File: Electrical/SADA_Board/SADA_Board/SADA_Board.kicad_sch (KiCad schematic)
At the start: 28 parts, among them J1 644752-2, U1 XC6230A001QR-G, U2 Si1442DH, U5 pico_shield

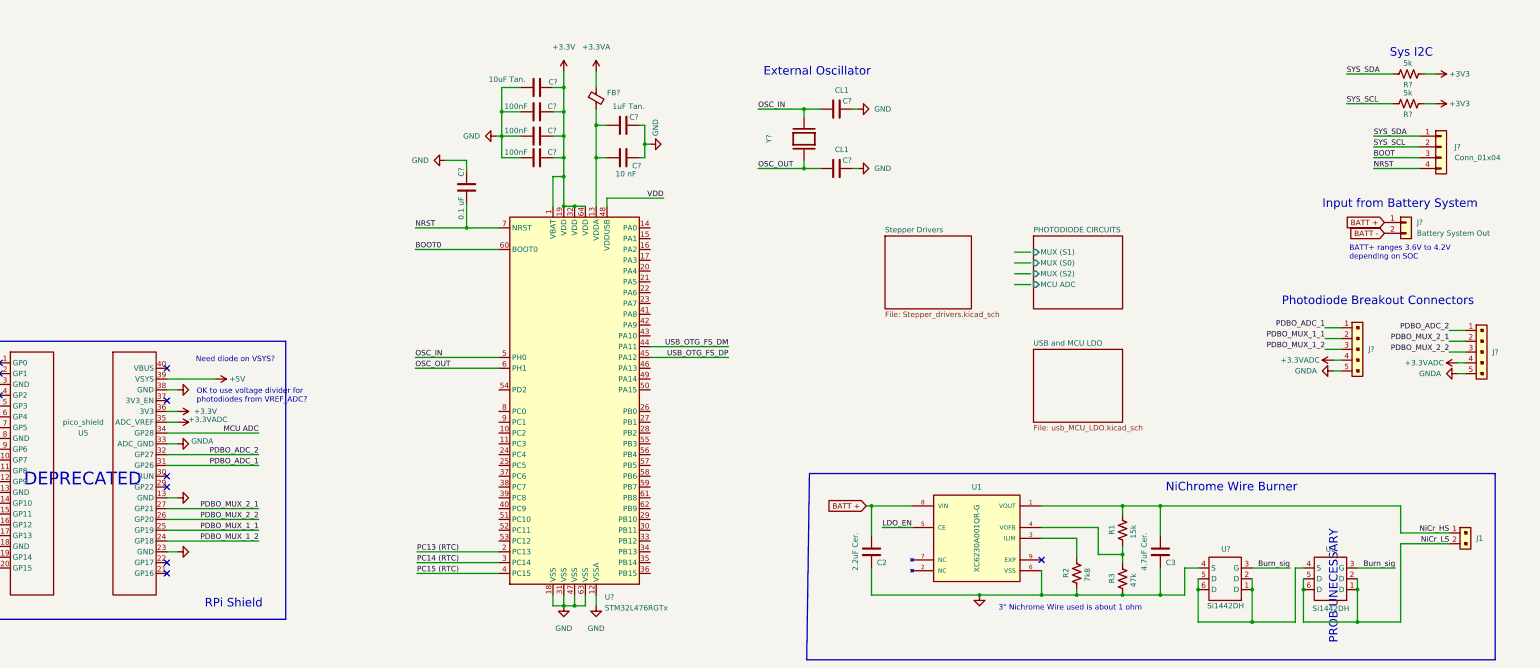
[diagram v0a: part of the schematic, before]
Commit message: Partial implementation of stepper motor Step up
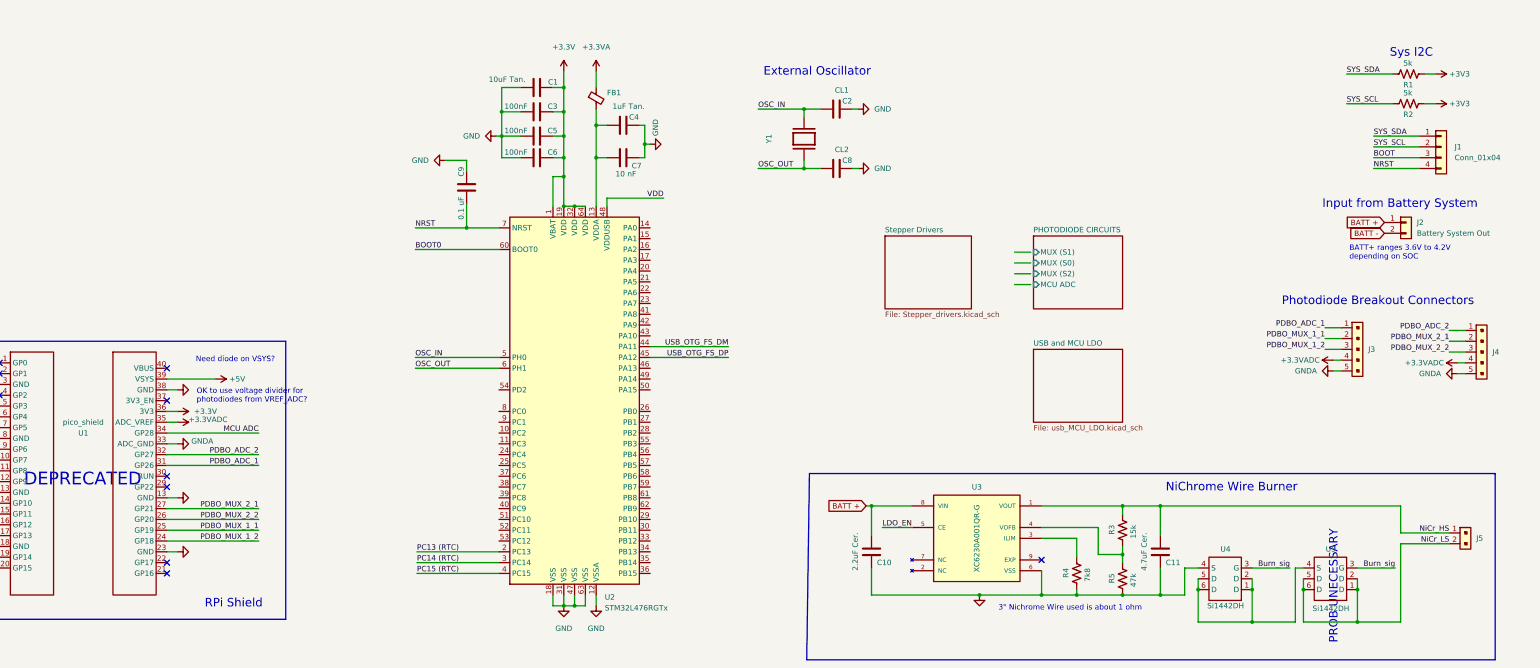
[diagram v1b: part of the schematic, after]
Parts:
- C8: renamed from C?; value CL1 -> CL2
- gave numbers to parts that had none: 18
- renumbered C2 to C10, C3 to C11, J1 to J5, R1 to R3, R2 to R4, R3 to R5, U5 to U1, U1 to U3, U2 to U5

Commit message: Rough draft stepup done
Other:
- note added: "TODO: - mosfet for stepper power (HS to keep ground connected) - Headers for all GPIO pins - Jumpers? - Hierarchal labels- may need to put 3V3 and others as global? - Connect grounds of System and SADA Board? Twisted pairs with ground? - current sensing? - Grounding Considerations... Do I just directly connect BATT- to ground or is there some sort of star grounding that should occur? future: - gi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"
- note removed: "TODO: - mosfet for stepper power (HS to keep ground connected) - Power considerations- input from battery/systems board, then filtering, then stepup. Standard - do things need to be at 5V other than stepper? maybe we could just use 3.3V - Stepper driver... is this final? what is the actual motor we are using? - Headers for all GPIO pins - Jumpers? - Hierarchal labels- may need to put 3V3 and othe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"

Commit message: Connectors, Oscillator
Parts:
- removed C3, C5: 100nF, Capacitor_SMD:C_0603_1608Metric, symbol Device:C
- removed C8: CL2, Capacitor_SMD:C_0603_1608Metric, symbol Device:C
- removed C9: 0.1 uF, Capacitor_SMD:C_0603_1608Metric, symbol Device:C
- removed FB1: FerriteBead_Small, symbol Device:FerriteBead_Small
- removed J1: Conn_01x04, symbol Connector_Generic:Conn_01x04
- removed J2: Battery System Out, symbol Connector_Generic:Conn_01x02
- removed J3, J4: B5B-XH-A_LF__SN_, digikey-footprints:PinHeader_1x5_P2.5mm_Drill1.1mm, symbol dk_Rectangular-Connectors-Headers-Male-Pins:B5B-XH-A_LF__SN_
- removed J5: 644752-2, digikey-footprints:PinHeader_1x2_P2mm_Drill1mm, symbol dk_Rectangular-Connectors-Headers-Male-Pins:B2B-PH-K-S_LF__SN_
- removed R2: 5k, symbol Device:R_US
- removed U1: pico_shield, symbol pi_pico_shield:pico_shield
- removed U5: Si1442DH, Package_TO_SOT_SMD:SOT-363_SC-70-6, symbol 0_custom:Si1442DH
- removed Y1: XRCGB48M000F5A00R0, OSC_XRCGB48M000F5A00R0, symbol XRCGB48M000F5A00R0:XRCGB48M000F5A00R0
- added C12: C, symbol Device:C
- added C? (x3): 100nF, Capacitor_SMD:C_0603_1608Metric, symbol Device:C
- added C?: CL2, Capacitor_SMD:C_0402_1005Metric, symbol Device:C
- added EXT? (x3): Male Conn., 0_custom:EXT_no_footprint, symbol 0_custom:{lt}name{gt}
- added J2, J? (x2): Conn_01x04, Miles Added:1719730004, symbol Connector_Generic:Conn_01x04
- added J?: 105431-1202, Miles Added:1054311202, symbol molex_105431-1202:105431-1202
- added R1: 4.7k, Resistor_SMD:R_0402_1005Metric, symbol Device:R_US
- added R6: r, symbol Device:R_US
- added Y?: ECS_Chrystal_, 0_custom:ECS-XTAL-5.0x3.2, symbol 0_custom:ECS_Chrystal_
- C1: MPN (none) -> F981A106MMUAJ6
- C10: footprint Capacitor_SMD:C_0805_2012Metric -> Capacitor_SMD:C_0603_1608Metric; MPN CL21B225KOFVPNE -> CGA3E1X7S1C225M080AC
- C11: footprint Capacitor_SMD:C_0805_2012Metric -> Capacitor_SMD:C_0603_1608Metric; MPN C2012X7R1A475K125AC -> GRT188C71C475KE13D
- C2: footprint Capacitor_SMD:C_0603_1608Metric -> Capacitor_SMD:C_0402_1005Metric; MPN (none) -> CGA2B2C0G1H060D050BA
- C4: MPN (none) -> TACL105K016XTA
- C6: MPN (none) -> C0603X104K3RAC7867
- R2: renamed from R1; value 5k -> 4.7k; footprint (none) -> Resistor_SMD:R_0402_1005Metric; MPN (none) -> AC0402FR-134K7L
- R3: footprint Resistor_SMD:R_0805_2012Metric_Pad1.20x1.40mm_HandSolder -> Resistor_SMD:R_0603_1608Metric; MPN RMCF0805FT15K8 -> AC0603FR-0715KL
- R4: value 7k8 -> 7.5k; footprint Resistor_SMD:R_0805_2012Metric_Pad1.20x1.40mm_HandSolder -> Resistor_SMD:R_0603_1608Metric_Pad0.98x0.95mm_HandSolder; MPN RC0805FR-077K87L -> AC0603FR-077K5L
- R5: footprint Resistor_SMD:R_0805_2012Metric_Pad1.20x1.40mm_HandSolder -> Resistor_SMD:R_0603_1608Metric; MPN RC0805FR-1347KL -> AC0603FR-1047KL
- renumbered U2 to U1, U3 to U2, U4 to U3
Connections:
- net VDD is gone; now on net +3.3V: U1.48 (VDDUSB)
- net +3.3V: now also C4.2, C7.2, U1.13 (VDDA), C?.1, C?.1
- net +3V3: now also J2.3 (Pin_3), J?.3 (Pin_3), R1.1
- net BOOT: now also J?.3 (Pin_3)
- net GND: now also C?.1, C?.1, C?.2, C?.2, J2.4 (Pin_4), J?.4 (Pin_4), J?.MP1, J?.MP2, Y?.2 (GND), Y?.4 (GND)
- net NRST: now also C?.2, J?.4 (Pin_4)
- net NiCr_HS: now also J?.1
- net NiCr_LS: now also U3.1 (D), U3.2 (D), U3.5 (D), U3.6 (D), J?.2
- net OSC_IN: now also Y?.3 (OUT/IN)
- net OSC_OUT: now also C?.2, Y?.1 (IN/OUT)
- net SYS_SCL: now also U1.58 (PB6), J?.1 (Pin_1), R1.2
- net SYS_SDA: now also U1.59 (PB7), J?.2 (Pin_2)
- net STEP_VREF2: now reaches U1.22 (PA6)
- net MTR2_DIR: now reaches U1.23 (PA7)
- net STEP_VREF1: now reaches U1.37 (PC6)
- net MTR1_STCK: now reaches U1.38 (PC7)
- net MTR1_DIR: now reaches U1.39 (PC8)
- net MTR1_FAULT: now reaches U1.40 (PC9)
- net MTR2_STCK: now reaches U1.41 (PA8)
- net MTR2_FAULT: now reaches U1.42 (PA9)
- net MTR2_STBY: now reaches U1.43 (PA10)
- net MTR1_STBY: now reaches U1.51 (PC10)
- new net PhDio_AUX_SCL: J2.1 (Pin_1), J?.1 (Pin_1)
- new net PhDio_AUX_SDA: J2.2 (Pin_2), J?.2 (Pin_2)
- no-connect marks 10 -> 1
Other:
- sheet PHOTODIODE CIRCUITS renamed CRNR PHOTODIODES
- removed sheet Stepper Drivers
- added sheet Steppers (Bipolar_Steppers.kicad_sch)
- sheet USB and MCU LDO ports: added USB_OTG_FS_DM, USB_OTG_FS_DP; removed none
- note added: "Passive Retainment NiChrome Burner"
- note added: "SCHEMATIC NOTES - See subpages for specific notes - BATT+ ranges 3.6V to 4.2V depending on SOC - Passive Retainment: 3" Nichrome Wire used is about 1 ohm"
- note added: "STM32 L476 MCU"
- note added: "TODO: - Headers for some GPIO pins - Jumpers? - Need to exchange ground with system board? - current sensing? - Star grounding? Ground loops anywhere? - grounding to chassis - SMD Shields"
- note added: "TODO: - update all connectors - find clock - power budget sheet - 3v3 LDO - USB Impedence - change aux photodiode board to i2c - double check flyback diodes on steppers"
- note removed: "3" Nichrome Wire used is about 1 ohm"
- note removed: "BATT+ ranges 3.6V to 4.2V depending on SOC"
- note removed: "DEPRECATED"
- note removed: "Input from Battery System"
- note removed: "Need diode on VSYS?"
- note removed: "NiChrome Wire Burner"
- note removed: "OK to use voltage divider for photodiodes from VREF_ADC?"
- note removed: "PROB UNECESSARY"
- note removed: "RPi Shield"
- note removed: "TODO: - mosfet for stepper power (HS to keep ground connected) - Headers for all GPIO pins - Jumpers? - Hierarchal labels- may need to put 3V3 and others as global? - Connect grounds of System and SADA Board? Twisted pairs with ground? - current sensing? - Grounding Considerations... Do I just directly connect BATT- to ground or is there some sort of star grounding that should occur? future: - gi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"
- moved on the sheet: C10, C11, C2, R2, R3, R4, R5, U2, U3

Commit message: Pre-Design Review II
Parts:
- removed C10: 2.2uF Cer., Capacitor_SMD:C_0603_1608Metric, symbol Device:C
- removed C11: 4.7uF Cer., Capacitor_SMD:C_0603_1608Metric, symbol Device:C
- removed C12: C, symbol Device:C
- removed J?: 105431-1202, Miles Added:1054311202, symbol molex_105431-1202:105431-1202
- removed R3: 15k, Resistor_SMD:R_0603_1608Metric, symbol Device:R_US
- removed R4: 7.5k, Resistor_SMD:R_0603_1608Metric_Pad0.98x0.95mm_HandSolder, symbol Device:R_US
- removed R5: 47k, Resistor_SMD:R_0603_1608Metric, symbol Device:R_US
- removed R6: r, symbol Device:R_US
- removed U2: XC6230A001QR-G, SOIC127P600X175-9N, symbol XC6230A001QR-G:XC6230A001QR-G
- removed U3: Si1442DH, Package_TO_SOT_SMD:SOT-363_SC-70-6, symbol 0_custom:Si1442DH
- added J?: Headers, Connector_PinSocket_2.00mm:PinSocket_2x30_P2.00mm_Vertical, symbol Connector_Generic:Conn_02x30_Counter_Clockwise
- added J?: Conn_01x05, Connector_PinSocket_2.00mm:PinSocket_1x05_P2.00mm_Vertical, symbol Connector_Generic:Conn_01x05
- J2: value Conn_01x04 -> Aux. Photodiode Board 1
- J?: value Conn_01x04 -> Systems Board Connector
- J?: value Conn_01x04 -> Aux. Photodiode Board 2
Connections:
- net PhDio_AUX_SCL is gone; now on net SYS_SCL: J2.1 (Pin_1), J?.1 (Pin_1)
- net PhDio_AUX_SDA is gone; now on net SYS_SDA: J2.2 (Pin_2), J?.2 (Pin_2)
- net +3V3: now also J?.47 (Pin_47), J?.48 (Pin_48)
- net BATT +: now also J?.12 (Pin_12), J?.13 (Pin_13)
- net BOOT0: now also J?.60 (Pin_60)
- net Burn_sig: now also U1.11 (PC3), J?.11 (Pin_11)
- net GND: now also J?.18 (Pin_18), J?.19 (Pin_19), J?.31 (Pin_31), J?.54 (Pin_54)
- net LDO_EN: now also U1.10 (PC2), J?.10 (Pin_10)
- net MTR1_DIR: now also J?.39 (Pin_39)
- net MTR1_FAULT: now also J?.40 (Pin_40)
- net MTR1_STBY: now also U1.36 (PB15), J?.36 (Pin_36); no longer U1.51 (PC10)
- net MTR1_STCK: now also J?.38 (Pin_38)
- net MTR2_DIR: now also U1.59 (PB7), J?.59 (Pin_59); no longer U1.23 (PA7)
- net MTR2_FAULT: now also U1.62 (PB9), J?.55 (Pin_55); no longer U1.42 (PA9)
- net MTR2_STBY: now also U1.57 (PB5), J?.57 (Pin_57); no longer U1.43 (PA10)
- net MTR2_STCK: now also U1.61 (PB8), J?.56 (Pin_56); no longer U1.41 (PA8)
- net MUX (S0): now also U1.27 (PB1), J?.27 (Pin_27)
- net MUX (S1): now also U1.28 (PB2), J?.28 (Pin_28)
- net MUX (S2): now also U1.25 (PC5), J?.25 (Pin_25)
- net NRST: now also J?.7 (Pin_7)
- net OSC_IN: now also J?.5 (Pin_5)
- net OSC_OUT: now also J?.6 (Pin_6)
- net PC13 (RTC): now also J?.2 (Pin_2)
- net PC14 (RTC): now also J?.3 (Pin_3)
- net PC15 (RTC): now also J?.4 (Pin_4)
- net STEP_VREF1: now also J?.37 (Pin_37)
- net STEP_VREF2: now also U1.58 (PB6), J?.58 (Pin_58); no longer U1.22 (PA6)
- net SYS_SCL: now also U1.8 (PC0), J?.8 (Pin_8); no longer U1.58 (PB6)
- net SYS_SDA: now also U1.9 (PC1), J?.9 (Pin_9); no longer U1.59 (PB7)
- net USB_OTG_FS_DM: now also J?.44 (Pin_44)
- net USB_OTG_FS_DP: now also J?.45 (Pin_45)
- net PA0: now reaches U1.14 (PA0)
- net PA0: now also J?.14 (Pin_14)
- net PA1: now reaches U1.15 (PA1)
- net PA1: now also J?.15 (Pin_15)
- net PA2: now reaches U1.16 (PA2)
- net PA2: now also J?.16 (Pin_16)
- net PA3: now reaches U1.17 (PA3)
- net PA3: now also J?.17 (Pin_17)
- net PA4: now reaches U1.20 (PA4)
- net PA4: now also J?.20 (Pin_20)
- net PA5: now reaches U1.21 (PA5)
- net PA5: now also J?.21 (Pin_21)
- net PC4: now reaches U1.24 (PC4)
- net PC4: now also J?.24 (Pin_24)
- net PhDio ADC: now reaches U1.26 (PB0)
- net PhDio ADC: now also J?.26 (Pin_26)
- net PB10: now reaches U1.29 (PB10)
- net PB10: now also J?.29 (Pin_29)
- net PB11: now reaches U1.30 (PB11)
- net PB11: now also J?.30 (Pin_30)
- net PB12: now reaches U1.33 (PB12)
- net PB12: now also J?.33 (Pin_33)
- net PB13: now reaches U1.34 (PB13)
- net PB13: now also J?.34 (Pin_34)
- net PB14: now reaches U1.35 (PB14)
- net PB14: now also J?.35 (Pin_35)
- net JTMS-SWDIO: now reaches U1.46 (PA13)
- net JTMS-SWDIO: now also J?.1 (Pin_1), J?.46 (Pin_46)
- net JTCK-SWCLK: now reaches U1.49 (PA14)
- net JTCK-SWCLK: now also J?.2 (Pin_2), J?.49 (Pin_49)
- net JTDI: now reaches U1.50 (PA15)
- net JTDI: now also J?.3 (Pin_3), J?.50 (Pin_50)
- net PC11: now reaches U1.52 (PC11)
- net PC11: now also J?.52 (Pin_52)
- net PC12: now reaches U1.53 (PC12)
- net PC12: now also J?.53 (Pin_53)
- net PD2: now reaches U1.54 (PD2)
- net JTDO - SWO: now reaches U1.55 (PB3)
- net JTDO - SWO: now also J?.4 (Pin_4)
- net NJTRST: now reaches U1.56 (PB4)
- net NJTRST: now also J?.5 (Pin_5)
- new net PA10: J?.43 (Pin_43), U1.43 (PA10)
- new net PA6: J?.22 (Pin_22), U1.22 (PA6)
- new net PA7: J?.23 (Pin_23), U1.23 (PA7)
- new net PA8: J?.41 (Pin_41), U1.41 (PA8)
- new net PA9: J?.42 (Pin_42), U1.42 (PA9)
- new net PC10: J?.51 (Pin_51), U1.51 (PC10)
- new net VDD: J?.1 (Pin_1), J?.32 (Pin_32)
- no-connect marks 1 -> 0
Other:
- sheet Steppers renamed Steppers 
- added sheet Passive Retainment (Passive_retainment.kicad_sch)
- note added: "Attitude Determination Photodiodes"
- note added: "Headers"
- note added: "JTAG/SWD"
- note added: "Passive Retainment"
- note added: "SCHEMATIC NOTES - See subpages for specific notes - BATT+ ranges 3.6V to 4.2V depending on SOC - Passive Retainment: 3" Nichrome Wire used is about 1 ohm - 'Headers' section will not be included on a final board, just for troubleshooting"
- note added: "Stepper Motors"
- note added: "System Board Interface"
- note added: "USB and 3V3 Power"
- note removed: "Passive Retainment NiChrome Burner"
- note removed: "SCHEMATIC NOTES - See subpages for specific notes - BATT+ ranges 3.6V to 4.2V depending on SOC - Passive Retainment: 3" Nichrome Wire used is about 1 ohm"
- note removed: "Sys I2C"
- note removed: "TODO: - Headers for some GPIO pins - Jumpers? - Need to exchange ground with system board? - current sensing? - Star grounding? Ground loops anywhere? - grounding to chassis - SMD Shields"
- note removed: "TODO: - update all connectors - find clock - power budget sheet - 3v3 LDO - USB Impedence - change aux photodiode board to i2c - double check flyback diodes on steppers"
- moved on the sheet: C2, C?, EXT?, J2, J?, R1, R2, Y?

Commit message: Pre-passive retainment change
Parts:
- removed C6, C? (x2): 100nF, Capacitor_SMD:C_0603_1608Metric, symbol Device:C
- added C? (x3): 100nF, Capacitor_SMD:C_0402_1005Metric, symbol Device:C
- C7: footprint Capacitor_SMD:C_0603_1608Metric -> Capacitor_SMD:C_0402_1005Metric; MPN (none) -> GRT155R71C103KE01J
- C?: footprint Capacitor_SMD:C_0603_1608Metric -> Capacitor_SMD:C_0402_1005Metric; MPN C0603X104K3RAC7867 -> GRT155R71C104KE01J
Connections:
- net +3.3V: now also C?.2, C?.2, C?.2
- net BOOT0: now also J?.31 (Pin_31); no longer J?.60 (Pin_60)
- net GND: now also J?.60 (Pin_60), C?.1, C?.1, C?.1; no longer J?.31 (Pin_31)
- net JTCK-SWCLK: no longer J?.49 (Pin_49)
- net JTDI: no longer J?.50 (Pin_50)
- net JTMS-SWDIO: no longer J?.46 (Pin_46)
- net SYS_SCL: now also J?.50 (Pin_50)
- net SYS_SDA: now also J?.49 (Pin_49)
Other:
- note added: "TODO: - USB research - GIO noise video - netlist check - passive retainment duplicate"

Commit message: pre-gio review
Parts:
- removed Y?: ECS_Chrystal_, 0_custom:ECS-XTAL-5.0x3.2, symbol 0_custom:ECS_Chrystal_
- added D1: TVS, symbol Diode:ESD5Zxx
- added D2, D3, D4, D5, D6, D7: TVS, Diode_SMD:D_0402_1005Metric, symbol Diode:ESD5Zxx
- added TP1, TP2, TP3, TP4: TestPoint, TestPoint:TestPoint_Pad_D1.5mm, symbol Connector:TestPoint
- added Y1: ECS_Chrystal_, Miles Added:XTAL_ECS-160-8-36Q-AES-TR, symbol 0_custom:ECS_Chrystal_
- gave numbers to parts that had none: 12
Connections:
- net +3.3V is gone; now on net +3V3: C1.1, C3.2, C4.2, C5.2, C6.2, C7.2, U1.1 (VBAT), U1.13 (VDDA), U1.19 (VDD), U1.32 (VDD), U1.48 (VDDUSB), U1.64 (VDD)
- net BOOT0 is gone; now on net BOOT: J1.31 (Pin_31), U1.60 (BOOT0)
- net +3V3: now also D1.1 (K)
- net BOOT: now also D3.1 (K)
- net GND: now also J1.46 (Pin_46), D1.2 (A), D2.2 (A), D3.2 (A), D4.2 (A), D5.2 (A), D6.2 (A), D7.2 (A), Y1.2 (GND), Y1.4 (GND); no longer J1.54 (Pin_54)
- net NRST: now also D2.1 (K)
- net OSC_IN: now also TP1.1, Y1.1 (IN/OUT)
- net OSC_OUT: now also TP2.1, Y1.3 (OUT/IN)
- net PD2: now also J1.54 (Pin_54)
- net SYS_SCL: now also D6.1 (K), TP3.1
- net SYS_SDA: now also D7.1 (K), TP4.1
- net USB_OTG_FS_DM: now also D4.1 (K)
- net USB_OTG_FS_DP: now also D5.1 (K)
- net LDO_EN renamed PR_EN
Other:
- sheet Passive Retainment ports: added PR_EN; removed LDO_EN
- note added: "TVS Diodes on clock?"
- note added: "TVS diodes? pins only used on ground charge could still build up though right?"
- note removed: "TODO: - USB research - GIO noise video - netlist check - passive retainment duplicate"
- title: CubeSat Pi Hat -> CubeSat SADA - Main
- moved on the sheet: C1, C3, C4, C5, C6, C7, C8, EXT3, J1, J5, R1, R2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

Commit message: ESD changes
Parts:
- added D28: LG_R971-KN-1, digikey-footprints:0805, symbol dk_LED-Indication-Discrete:LG_R971-KN-1
- added H1, H2, H3, H4: MountingHole_Pad, MountingHole:MountingHole_2.5mm_Pad, symbol Mechanical:MountingHole_Pad
- added JP1: Jumper_3_Open, Connector_PinHeader_2.54mm:PinHeader_1x03_P2.54mm_Vertical_SMD_Pin1Right, symbol Jumper:Jumper_3_Open
- added R31: 4.7k, Resistor_SMD:R_0402_1005Metric, symbol Device:R_US
- D1: footprint (none) -> Diode_SMD:D_0402_1005Metric; MPN (none) -> ESD321DPYR
- TP1, TP2, TP3, TP4: footprint TestPoint:TestPoint_Pad_D1.5mm -> TestPoint:TestPoint_Pad_D1.0mm
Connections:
- net +3V3: now also D28.1, JP1.3 (B)
- net BOOT: now also R31.1
- net GND: now also D28.2, H1.1, H2.1, H3.1, H4.1, JP1.1 (A)
- new net: JP1.2 (C), R31.2
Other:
- note added: "PWR LED"
- moved on the sheet: D3
